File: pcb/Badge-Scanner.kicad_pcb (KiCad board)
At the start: 2 copper layers, 75 x 52 mm, 39 parts, among them J1 I2C, J2 NFC-Module, J3 Buzzer, J4 Micro_SD_Card_Det1, Q1 2N7002, Q2 2N7002, Q3 AO3400A, U1 Pico W, U2 DS3231MZ

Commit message: style: add JLC order number position
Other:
- board text added: "JLCJLCJLCJLC"
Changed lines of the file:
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@@
+		)
+	)
+	(gr_text "JLCJLCJLCJLC"
+		(at 147 117.5 90)
+		(layer "F.SilkS")
+		(effects
+			(font
+				(size 0.8 0.8)
+				(thickness 0.15)
+			)
+			(justify left bottom)
 		)
 	)

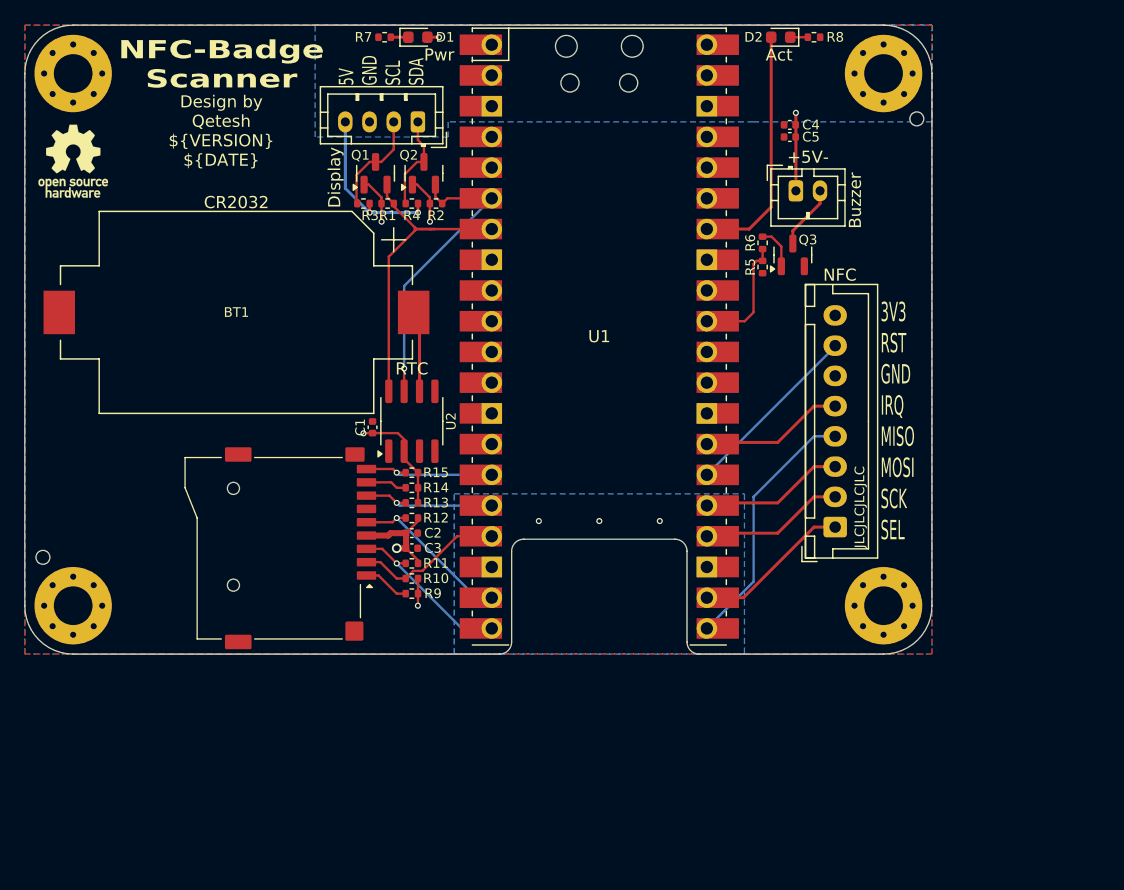
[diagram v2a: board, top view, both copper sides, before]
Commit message: feat: add LiPo Circuitry
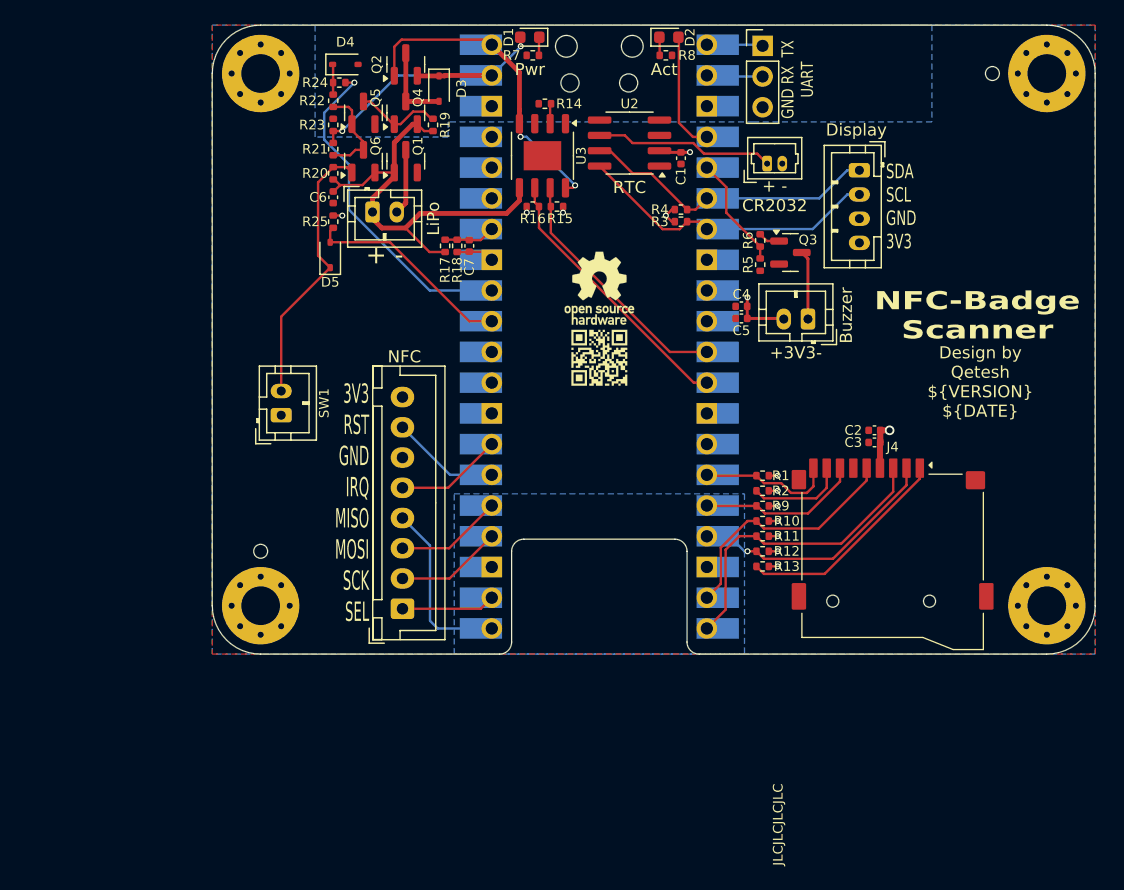
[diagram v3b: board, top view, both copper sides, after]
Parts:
- added BT2: 18650, Connector_JST:JST_PH_B2B-PH-K_1x02_P2.00mm_Vertical, F.Cu at (106.2, 89.7)
- added C6: 10u, Capacitor_SMD:C_0402_1005Metric, F.Cu at (103.0, 88.5)
- added C7: 100n, Capacitor_SMD:C_0402_1005Metric, F.Cu at (114.2, 92.5)
- added D3: 1N5819WS, Diode_SMD:D_SOD-323, F.Cu at (111.8, 79.5)
- added D4: MM3Z3V0, Diode_SMD:D_SOD-323, F.Cu at (104.0, 77.5)
- added D5: 1N5819WS, Diode_SMD:D_SOD-323, F.Cu at (102.8, 93.2)
- added G***: LOGO, My_Footprints:qr_qete.sh-el_05, F.Cu at (125.0, 101.8)
- added J5: Serial, Connector_PinHeader_2.54mm:PinHeader_1x03_P2.54mm_Vertical, F.Cu at (138.5, 76.0)
- added Q4: AO3401A, Package_TO_SOT_SMD:SOT-23, F.Cu at (109.0, 81.5)
- added Q5: AO3400A, Package_TO_SOT_SMD:SOT-23, F.Cu at (105.5, 81.5)
- added Q6: AO3401A, Package_TO_SOT_SMD:SOT-23, F.Cu at (105.5, 85.5)
- added R16: 10k, Resistor_SMD:R_0402_1005Metric, F.Cu at (119.5, 89.2)
- added R17: 10M, Resistor_SMD:R_0402_1005Metric, F.Cu at (112.2, 92.5)
- added R18: 10M, Resistor_SMD:R_0402_1005Metric, F.Cu at (113.2, 92.5)
- added R19: 1M, Resistor_SMD:R_0402_1005Metric, F.Cu at (111.2, 82.5)
- added R20: 100k, Resistor_SMD:R_0402_1005Metric, F.Cu at (103.0, 86.5)
- added R21: 1M, Resistor_SMD:R_0402_1005Metric, F.Cu at (103.0, 84.5)
- added R22: 10k, Resistor_SMD:R_0402_1005Metric, F.Cu at (103.0, 80.5)
- added R23: 100k, Resistor_SMD:R_0402_1005Metric, F.Cu at (103.0, 82.5)
- added R24: 10k, Resistor_SMD:R_0402_1005Metric, F.Cu at (103.5, 79.0)
- added R25: 100k, Resistor_SMD:R_0402_1005Metric, F.Cu at (103.0, 90.5)
- added SW1: Power, Connector_JST:JST_PH_B2B-PH-K_1x02_P2.00mm_Vertical, F.Cu at (98.7, 106.5)
- added U3: TP4056, Package_SO:HSOP-8-1EP_3.9x4.9mm_P1.27mm_EP2.41x3.1mm, F.Cu at (120.3, 85.0)
- BT1: footprint Battery:BatteryHolder_Keystone_1060_1x2032 -> Connector_Molex:Molex_PicoBlade_53047-0210_1x02_P1.25mm_Vertical
- C1, C5: value 100nF -> 100n
- C2: value 100nF -> 10u
- C3: value 10uF -> 100n
- C4: value 10uF -> 10u
- Q1: value 2N7002 -> AO3400A
- Q2: value 2N7002 -> AO3401A
- R1, R2: value 4k7 -> 3k3
- R14: value 3k3 -> 2k
- R15: value 3k3 -> 10k
- R3, R4: value 4k7 -> 2k2
- U1: moved to B.Cu
- moved J4 54.7 mm to (149.2, 121.9), turned to 0 degrees
- moved BT1 45.6 mm to (138.9, 85.7), turned to 0 degrees
- moved REF** 44.7 mm to (125.0, 96.0)
- moved C3 39.2 mm to (147.8, 108.8), turned to 0 degrees
- moved C2 39.2 mm to (147.8, 107.8), turned to 0 degrees
- moved R1 38.3 mm to (138.5, 111.5)
- moved J1 36.7 mm to (146.5, 86.2), turned to -90 degrees
- moved J2 36.4 mm to (108.7, 122.5)
- moved R2 36.0 mm to (138.5, 112.8)
- moved C1 33.8 mm to (131.8, 85.2), turned to 90 degrees
- moved R14 33.6 mm to (120.5, 80.8)
- moved R9 29.9 mm to (138.5, 114.0)
- moved R13 29.5 mm to (138.5, 119.0)
- moved R10 29.4 mm to (138.5, 115.2)
- moved U2 29.2 mm to (127.5, 84.0), turned to 180 degrees
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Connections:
- net /VBAT renamed /RTC_VBAT
- C4 pad 2: +5V -> +3V3
- C5 pad 2: +5V -> +3V3
- D1 pad 2: +5V -> VSYS
- J1 pad 1: /SDA_5V -> /SDA
- J1 pad 2: /SCL_5V -> /SCL
- J1 pad 4: +5V -> +3V3
- J3 pad 1: +5V -> /BzrOut
- J3 pad 2: /BzrOut -> +3V3
- J4 pad 1: /DAT2 -> /SDCard/DAT2
- J4 pad 8: /DAT1 -> /SDCard/DAT1
- Q1 pad 1: +3V3 -> /Battery Management/Batt+
- Q1 pad 2: /SCL -> GND
- Q1 pad 3: /SCL_5V -> /Battery Management/Batt-
- Q2 pad 1: +3V3 -> VBUS
- Q2 pad 2: /SDA -> VSYS
- Q2 pad 3: /SDA_5V -> /Battery Management/BattSwd
- R1 pad 1: /SCL -> +3V3
- R1 pad 2: +3V3 -> /SD_DET
- R10 pad 2: /SD_CS -> /SD_SCK
- R12 pad 2: /SD_SCK -> /SD_CS
- R13 pad 2: /SD_MISO -> /SDCard/DAT2
- R14 pad 1: +3V3 -> /Battery Management/PROG
- R14 pad 2: /DAT1 -> GND
- R15 pad 2: /SD_DET -> /~{ChargeActive}
- R2 pad 1: /SDA -> +3V3
- R2 pad 2: +3V3 -> /SDCard/DAT1
- R3 pad 1: /SCL_5V -> /SCL
- R3 pad 2: +5V -> +3V3
- R4 pad 1: /SDA_5V -> /SDA
- R4 pad 2: +5V -> +3V3
- R9 pad 2: /DAT2 -> /SD_MISO
- U1 pad 1: unconnected-(U1-GP0-Pad1) -> /UART0TX
- U1 pad 11: unconnected-(U1-GP8-Pad11)_0 -> /~{ChargeActive}
- U1 pad 12: unconnected-(U1-GP9-Pad12) -> /~{ChargeStdby}
- U1 pad 2: unconnected-(U1-GP1-Pad2)_0 -> /UART0RX
- U1 pad 31: /Buzzer -> /~{PwrButton}
- U1 pad 32: unconnected-(U1-GP27-Pad32)_0 -> /~{BattPwrOff}
- U1 pad 33: GND -> GNDA
- U1 pad 34: /LED -> /BattMeas
- U1 pad 39: +5V -> VSYS
- U1 pad 4: unconnected-(U1-GP2-Pad4) -> /LED
- U1 pad 40: +5V -> VBUS
- U1 pad 5: unconnected-(U1-GP3-Pad5)_0 -> /Buzzer
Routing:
- net /Battery Management/Batt+: track 0.00 -> 35.9 mm
- net /~{BattPwrOff}: track 0.00 -> 27.8 mm, vias 0 -> 1
- net VBUS: track 0.00 -> 26.5 mm, vias 0 -> 2
- net VSYS: track 0.00 -> 26.4 mm, vias 0 -> 2
- net Net-(D5-K): track 0.00 -> 22.9 mm
- net /~{ChargeStdby}: track 0.00 -> 22.6 mm
- net +5V: track 21.2 -> 0.00 mm, vias 4 -> 0
- net /~{ChargeActive}: track 0.00 -> 20.7 mm
- net /SDCard/DAT2: track 0.00 -> 17.9 mm
- net /~{PwrButton}: track 0.00 -> 17.4 mm
- net /SD_MOSI: track 13.8 -> 25.5 mm, vias 1 -> 0
- net /LED: track 20.2 -> 9.89 mm
- net /SD_CS: track 12.4 -> 21.2 mm, vias 0 -> 1
- net /SCL_5V: track 8.61 -> 0.00 mm
- net /SDCard/DAT1: track 0.00 -> 8.06 mm
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- removed copper zone on B.Cu, net +5V
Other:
- board size 75 x 52 mm -> 73 x 52 mm
- board text added: "+ -"
- board text added: "+ - CR2032"
- board text added: "+3V3-"
- board text added: "0 UART TX 1 UART RX 2 LED 3 Buzzer 4 I2C SDA 5 I2C SDL 8 Charge Active 9 Charge Standby 11 SD DET 12 SD MISO 13 SD CS 14 SD SCK 15 SD MOSI 16 NFC MISO 17 NFC CS 18 NFC SCK 19 NFC MOSI 20 NFC RST 21 NFC IRQ 26 Power Button 27 Power Off 28 Battery Voltage"
- board text added: "GND RX TX UART"
- board text added: "LiPo"
- board text added: "SDA SCL GND 3V3"
- board text added: "Todo: Move Rpi to bottom of pcb"
- board text removed: "+5V-"
- board text removed: "4 I2C SDA 5 I2C SDL 11 SD DET 12 SD MISO 13 SD CS 14 SD SCK 15 SD MOSI 16 NFC MISO 17 NFC CS 18 NFC SCK 19 NFC MOSI 20 NFC RST 21 NFC IRQ 26 Buzzer 28 Act-LED"
- board text removed: "5V GND SCL SDA"
- board text removed: "CR2032"

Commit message: style: silk screen cleanup
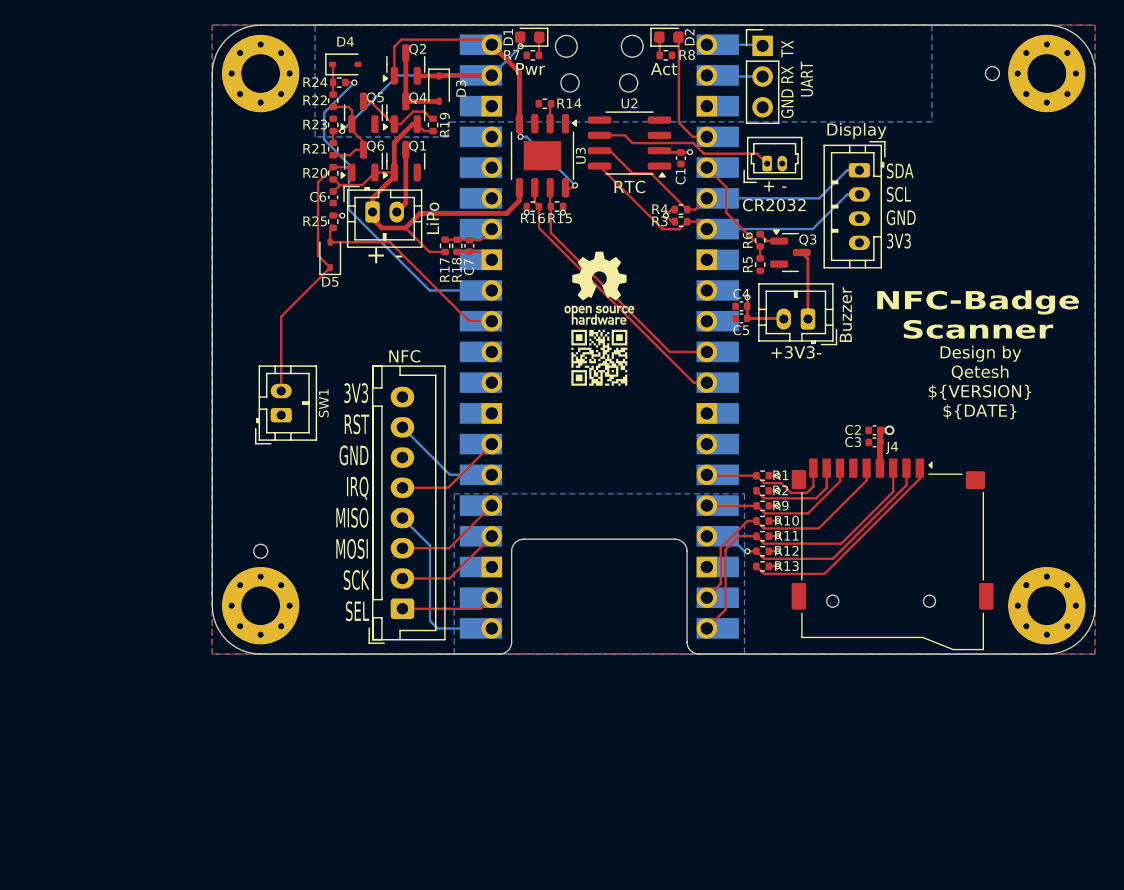
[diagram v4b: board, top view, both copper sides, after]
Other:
- board text removed: "JLCJLCJLCJLC"
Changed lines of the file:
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@@
 		(tags "resistor")
 		(property "Reference" "R22"
-			(at 0 -1.75 180)
+			(at 0 -1.5 180)
 			(layer "F.SilkS")
 			(effects
@@
 		(tags "SOT TO_SOT_SMD")
 		(property "Reference" "Q5"
-			(at 1.25 1 90)
+			(at 1.25 1 180)
 			(layer "F.SilkS")
 			(effects
@@
 		(tags "SOT TO_SOT_SMD")
 		(property "Reference" "Q2"
-			(at 0 -2.4 90)
+			(at 1.25 1 180)
 			(layer "F.SilkS")
 			(effects
@@
 		(tags "SOT TO_SOT_SMD")
 		(property "Reference" "Q4"
-			(at 1.25 1 90)
+			(at 1.25 1 180)
 			(layer "F.SilkS")
 			(effects
@@
 			(thermal_bridge_angle 45)
 		)
+		(model "${KIPRJMOD}/MicroSDSocket.step"
+			(offset
+				(xyz -120.8 50.4 -196.8)
+			)
+			(scale
+				(xyz 1 1 1)
+			)
+			(rotate
+				(xyz 0 0 180)
+			)
+		)
 	)
 	(footprint "MountingHole:MountingHole_3.2mm_M3_Pad_Via"
@@
 		(tags "SOT TO_SOT_SMD")
 		(property "Reference" "Q6"
-			(at 1.25 1 90)
+			(at 1.25 1 180)
 			(layer "F.SilkS")
 			(effects
@@
 		(tags "SOT TO_SOT_SMD")
 		(property "Reference" "Q1"
-			(at 1.25 1 90)
+			(at 1.25 1 180)
 			(layer "F.SilkS")
 			(effects
@@
 		(tags "resistor")
 		(property "Reference" "R23"
-			(at 0 -1.75 180)
+			(at 0 -1.5 180)
 			(layer "F.SilkS")
 			(effects
@@
 		)
 	)
-	(gr_text "JLCJLCJLCJLC"
-		(at 140.25 143.75 90)
-		(layer "F.SilkS")
-		(effects
-			(font
-				(size 0.8 0.8)
-				(thickness 0.15)
-			)
-			(justify left bottom)
-		)
-	)

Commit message: fix: replace buzzer footprint
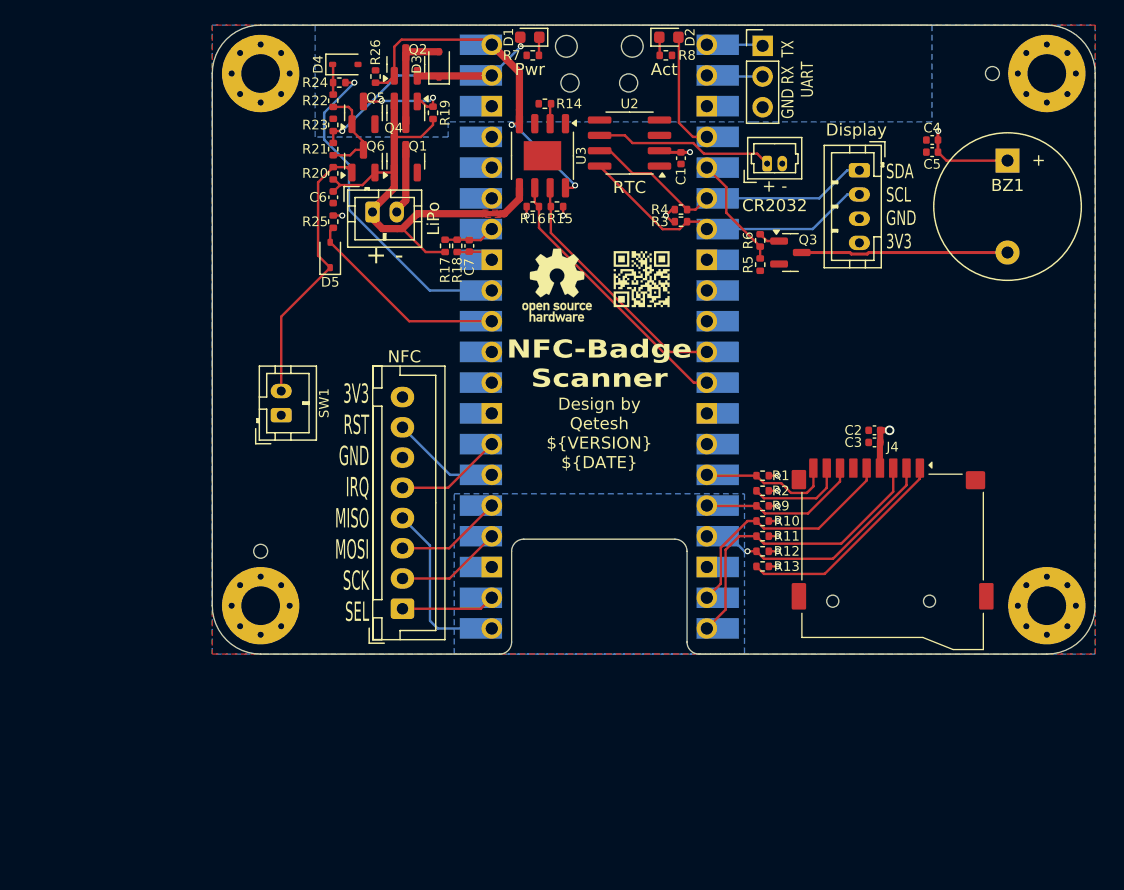
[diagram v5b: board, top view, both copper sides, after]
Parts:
- removed J3: Buzzer, Connector_JST:JST_PH_B2B-PH-K_1x02_P2.00mm_Vertical
- added BZ1: Buzzer, Buzzer_Beeper:Buzzer_12x9.5RM7.6, F.Cu at (158.8, 85.5)
- added R26: 100k, Resistor_SMD:R_0402_1005Metric, F.Cu at (106.5, 78.5)
- moved C4 20.9 mm to (152.5, 83.8)
- moved C5 20.9 mm to (152.5, 84.8)
- moved G*** 7.38 mm to (128.5, 95.2)
- moved REF** 3.51 mm to (121.5, 95.8)
- moved D3 2.00 mm to (111.8, 77.5), turned to 90 degrees
- moved R19 1.00 mm to (111.2, 81.5)
- turned Q4 to -90 degrees
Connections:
- net Net-(D5-K) renamed /Battery Management/SW1
- Q3 pad 3: /BzrOut -> /BZ-
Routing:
- net /BZ-: track 0.00 -> 17.1 mm
- net /BzrOut: track 5.71 -> 0.00 mm
- net /Battery Management/Batt+: track 35.9 -> 39.7 mm
- net +3V3: track 20.1 -> 23.6 mm
- net VBUS: track 26.5 -> 29.0 mm
- net /Battery Management/BattSwd: track 6.71 -> 8.67 mm
- net /Battery Management/BattSwG: track 7.05 -> 8.10 mm, vias 0 -> 2
- added copper zone on F.Cu, net /Battery Management/Batt+
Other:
- board text removed: "+3V3-"
- board text removed: "Buzzer"

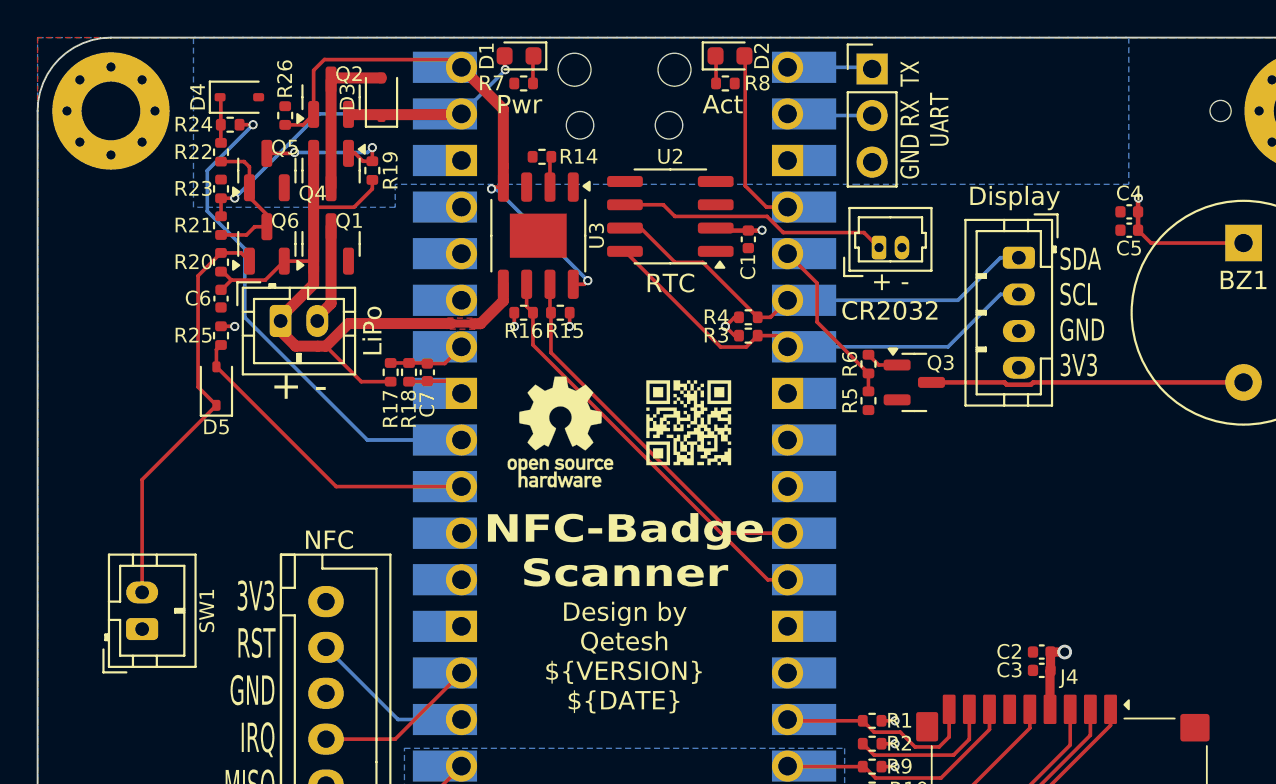
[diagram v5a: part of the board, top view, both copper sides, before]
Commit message: feat: place power button on the board
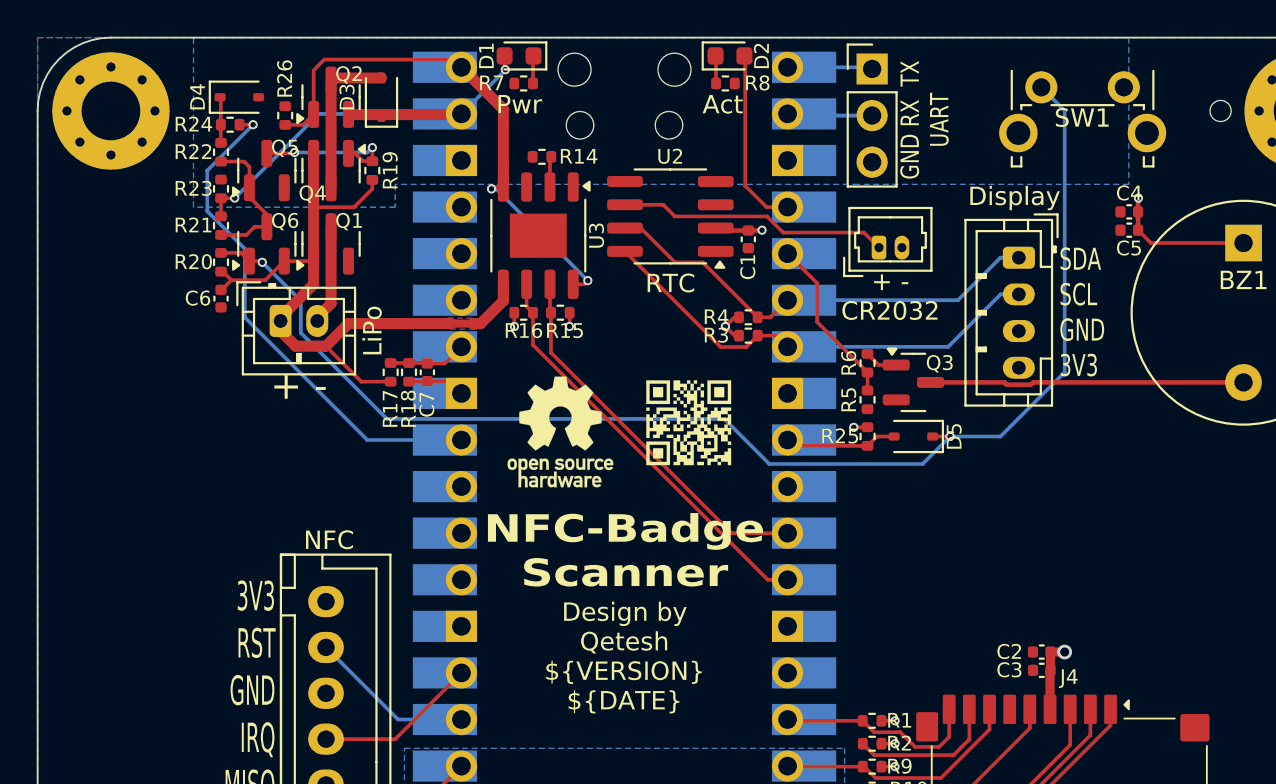
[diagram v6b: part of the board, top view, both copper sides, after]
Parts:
- SW1: footprint Connector_JST:JST_PH_B2B-PH-K_1x02_P2.00mm_Vertical -> Button_Switch_THT:SW_Tactile_SPST_Angled_PTS645Vx58-2LFS
- moved SW1 57.2 mm to (147.7, 77.0), turned to 0 degrees
- moved D5 38.1 mm to (140.8, 96.0), turned to 180 degrees
- moved R25 35.7 mm to (138.2, 96.0)
- moved R5 0.07 mm to (138.2, 94.0)
- moved R6 0.07 mm to (138.2, 92.0)
- moved Q3 0.05 mm to (140.8, 93.0)
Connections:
- SW1 pad 1: GND -> /Battery Management/SW1
- SW1 pad 2: /Battery Management/SW1 -> GND
- U1 pad 31: /~{PwrButton} -> unconnected-(U1-GP26-Pad31)
- U1 pad 9: unconnected-(U1-GP6-Pad9)_1 -> /~{PwrButton}
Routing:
- net /Battery Management/SW1: track 22.9 -> 70.9 mm, vias 0 -> 2
- net /~{PwrButton}: track 17.4 -> 6.15 mm
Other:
- board text added: "0 UART TX 1 UART RX 2 LED 3 Buzzer 4 I2C SDA 5 I2C SDL 6 Power Button 8 Charge Active 9 Charge Standby 27 Power Off 28 Battery Voltage"
- board text added: "11 SD DET 12 SD MISO 13 SD CS 14 SD SCK 15 SD MOSI 16 NFC MISO 17 NFC CS 18 NFC SCK 19 NFC MOSI 20 NFC RST 21 NFC IRQ"
- board text removed: "0 UART TX 1 UART RX 2 LED 3 Buzzer 4 I2C SDA 5 I2C SDL 8 Charge Active 9 Charge Standby 11 SD DET 12 SD MISO 13 SD CS 14 SD SCK 15 SD MOSI 16 NFC MISO 17 NFC CS 18 NFC SCK 19 NFC MOSI 20 NFC RST 21 NFC IRQ 26 Power Button 27 Power Off 28 Battery Voltage"
